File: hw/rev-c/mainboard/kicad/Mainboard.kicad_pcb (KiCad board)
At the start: 2 copper layers, 262.5 x 95.2 mm, 270 parts, among them J1 IEEE, J10 5V PWR, J11 9V POWER, J12 9V POWER, J13 CASS_B_HEADER, J14 IEEE_HEADER, J15 KEYBOARD_EX, J16 USER_HEADER, J17 PMOD1, J18 PMOD2, J19 PROG, J2 USER, J20 CASS_A_HEADER, J21 NOT_HDMI_A, J22 AUDIO, J23 MICRO_SD, J24 USB1.1_HOST_TYPE_C, J25 MENU, J3 CASS A, J4 BUS_EXPANSION, J5 KEYBOARD, J6 CASS B, J7 VIDEO, J8 PET POWER, J9 FPGA_MCU, Q1 MMBT3904, Q2 AO3401A, Q3 AO3401A, SW1 RESET, SW2 NMI, SW3 CONFIG, SW4 RUN, SW5 MENU, SW6 BOOTSEL, U1 W65C02S, U10 T8Q144C3, U11 W65C21N, U12 W65C21N, U13 W65C22N, U14 SN74LS07, U15 SN74LS07, U16 SN74LS07, U17 74LS245, U18 74LS245, U19 74LS145, U2 AS6C1008, U20 LM386, U21 RP2040, U22 W25Q128JVS, U3 AMS1117-3.3, U4 XL1509-5.0E1, U5 LM317AG-TN3-R, U6 LM317AG-TN3-R, U7 SN74LVC4245APWR, U8 SN74LVC4245APWR, U9 SN74LVC4245APWR, Y1 12 MHz

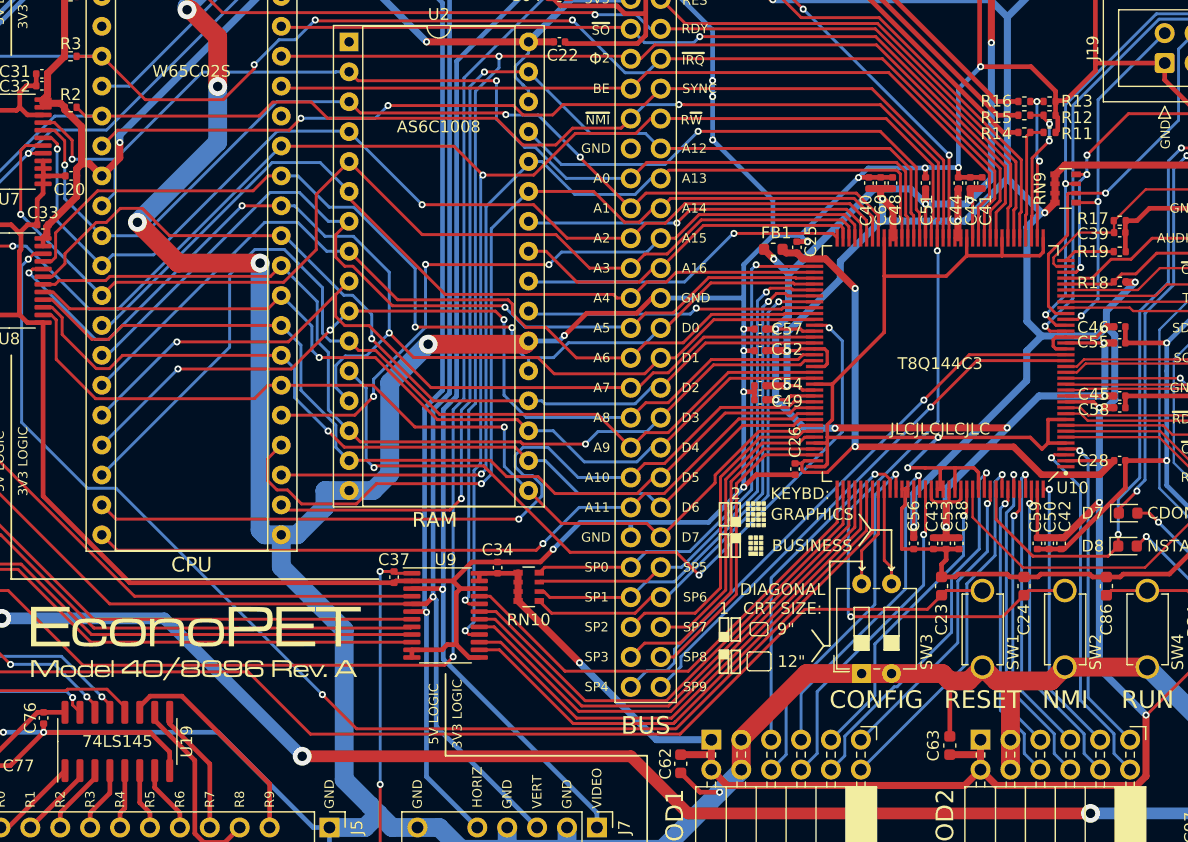
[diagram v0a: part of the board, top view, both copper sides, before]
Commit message: hw(rev-c): reroute ram_a10
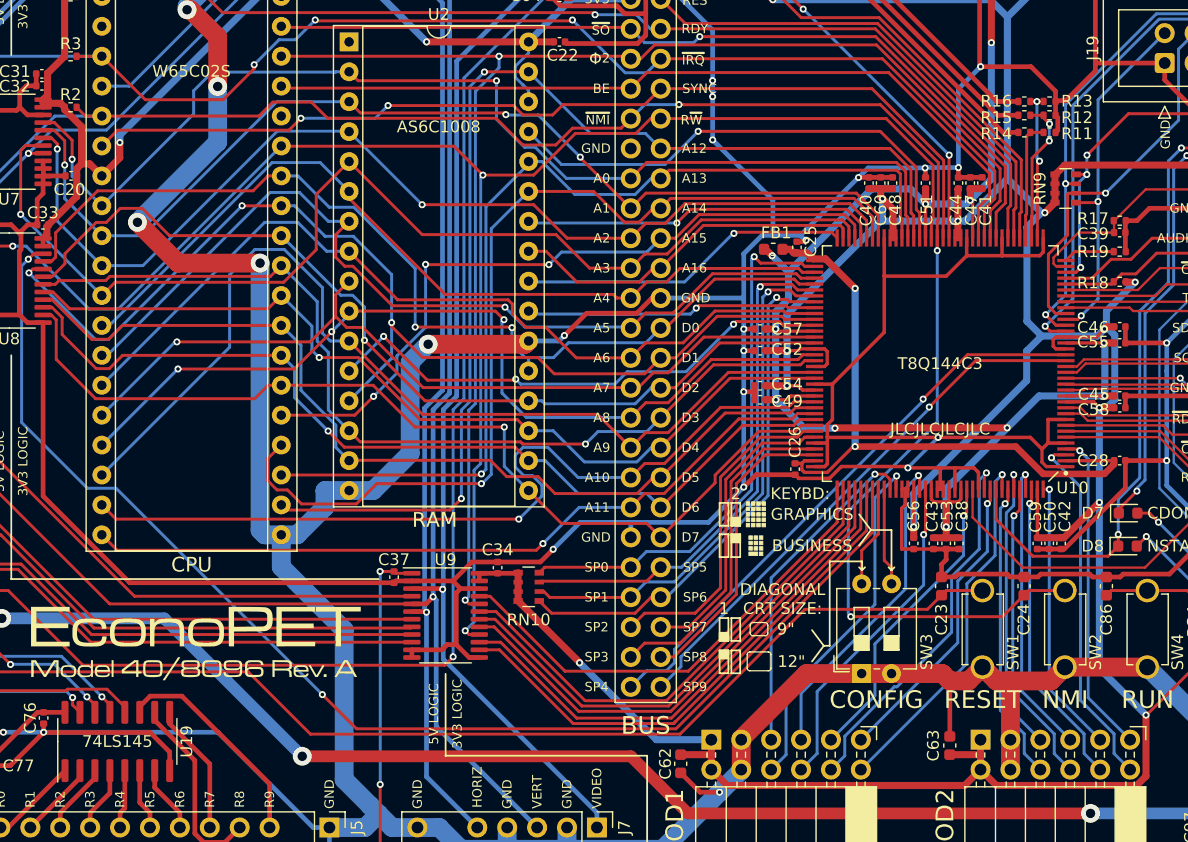
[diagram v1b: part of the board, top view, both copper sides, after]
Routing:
- net /CPU \ RAM/RAM_A10: track 68.4 -> 44.8 mm
- net GND: track 2307.3 -> 2321.0 mm
- net /CPU \ RAM/D1: track 95.1 -> 93.8 mm
- net /MAGIC/FPGA/~{TEST}: track 45.2 -> 46.3 mm
- net /CPU \ RAM/A0: track 95.2 -> 96.1 mm
- net /MAGIC/FPGA/CBUS0: track 43.2 -> 44.1 mm
- net /CPU \ RAM/A7: track 72.5 -> 71.8 mm
- net /MAGIC/FPGA/CBUS1: track 43.6 -> 44.4 mm
- net /MAGIC/FPGA/CBUS2: track 43.9 -> 44.5 mm

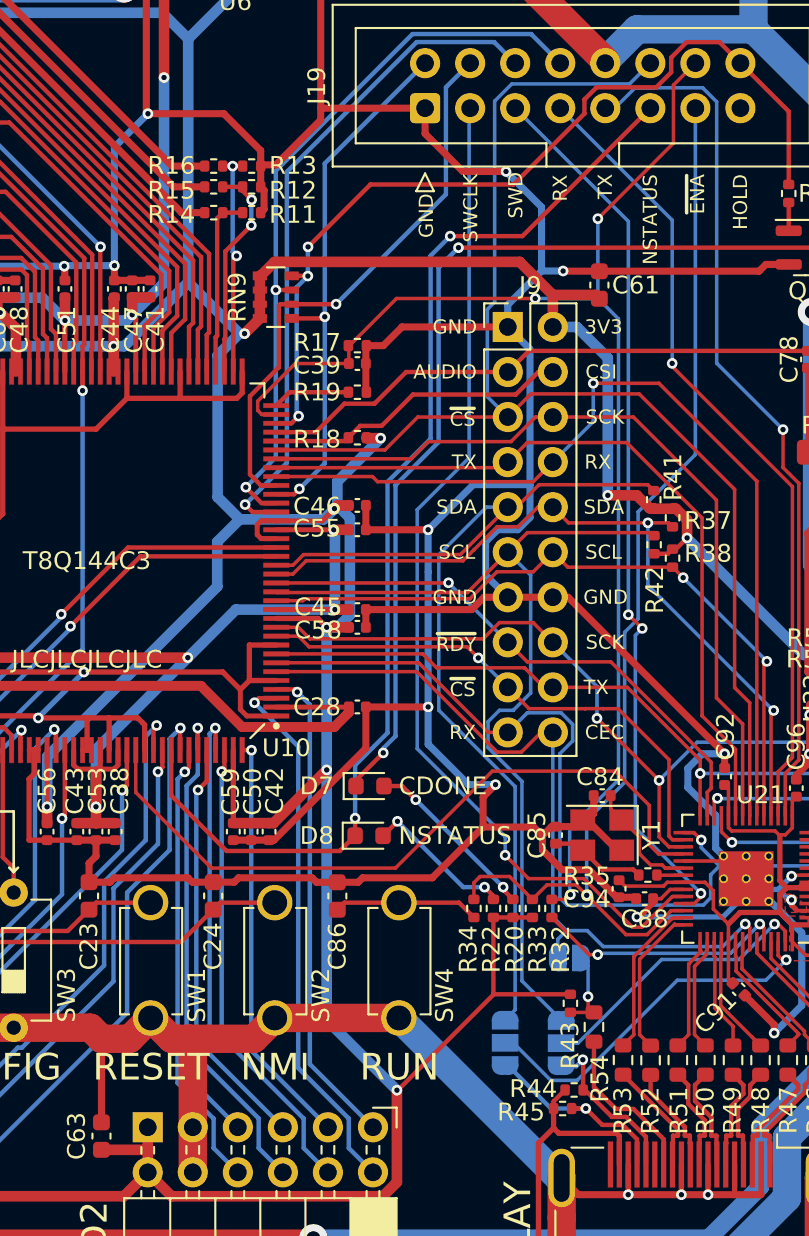
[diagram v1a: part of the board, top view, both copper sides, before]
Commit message: hw(rev-c): touch up routing
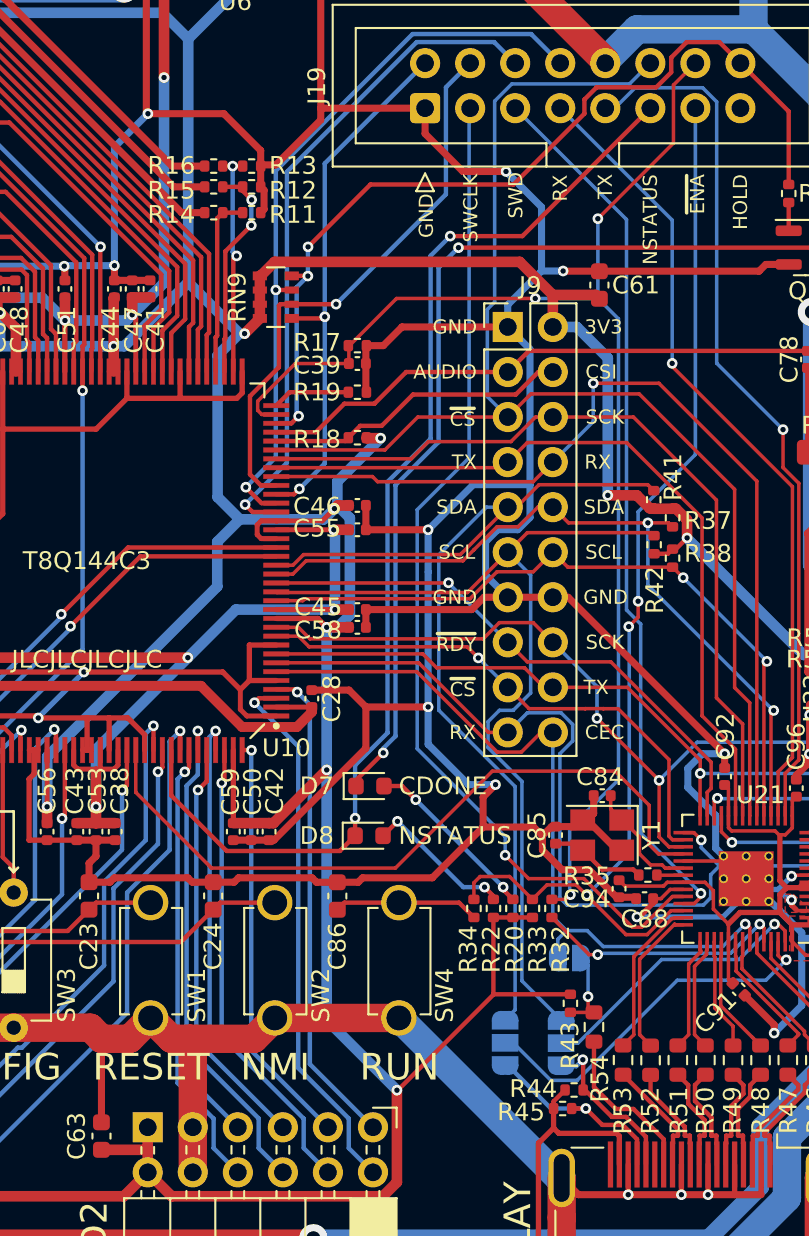
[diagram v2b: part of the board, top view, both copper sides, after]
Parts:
- moved C28 2.61 mm to (298.6, 152.5), turned to 90 degrees
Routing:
- net FPGA_VCCA: track 56.5 -> 52.3 mm
- net GND: track 2321.0 -> 2324.1 mm
- net /MAGIC/FPGA/SWD: track 50.3 -> 50.0 mm, vias 3 -> 1
- net /MAGIC/FPGA/~{SPI_ENA}: vias 1 -> 3
